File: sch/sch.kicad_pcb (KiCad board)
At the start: 2 copper layers, 98.6 x 49.8 mm, 106 parts, among them P1 SWD, P10 Button_on, P11 LiFePo4, P12 3.3v, P13 SPEAKR, P14 RESET, P15 GPS_UART0, P2 UART, P3 usb, P4 btns1, P5 Leds_gnd, P6 btns2, P7 Leds, P8 3V_bat, P9 LCD, Q1 Q_PMOS_GSD, Q2 Q_PMOS_GSD, Q3 Q_NMOS_DSG, SW1 SW_PUSH, U1 24C512, U10 STMPS2141STR, U11 MCP73123, U12 LT1613, U13 74LVC1G17, U14 74LVC2G74, U15 74LVC1G02, U16 NCP1450, U17 microSD, U2 STM32F401RETx, U3 74HC595, U4 LSM303D, U5 ML8088se, U6 GPS_ANTENNA, U7 INA138, U8 INA138, U9 74LVC1G32, Y1 8MHz, Y2 32768

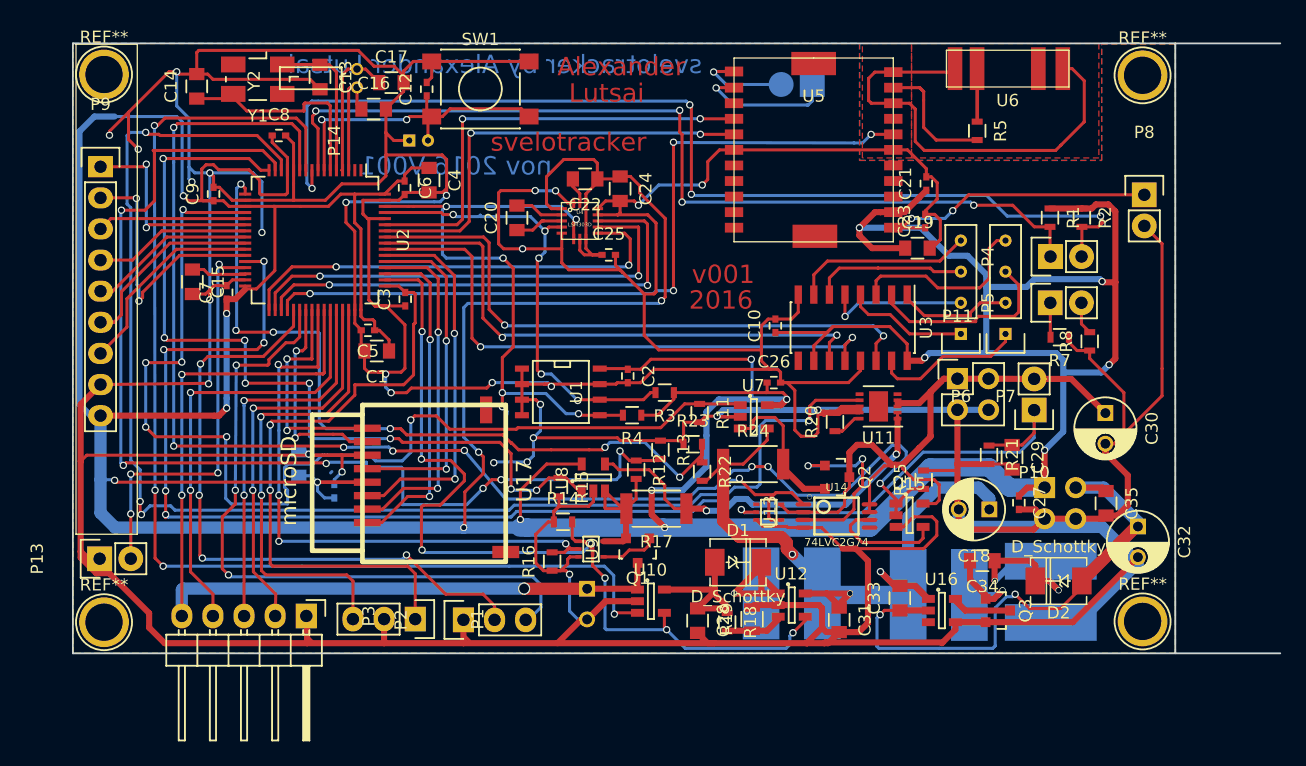
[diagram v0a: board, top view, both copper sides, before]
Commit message: sd card 180 degree rotation
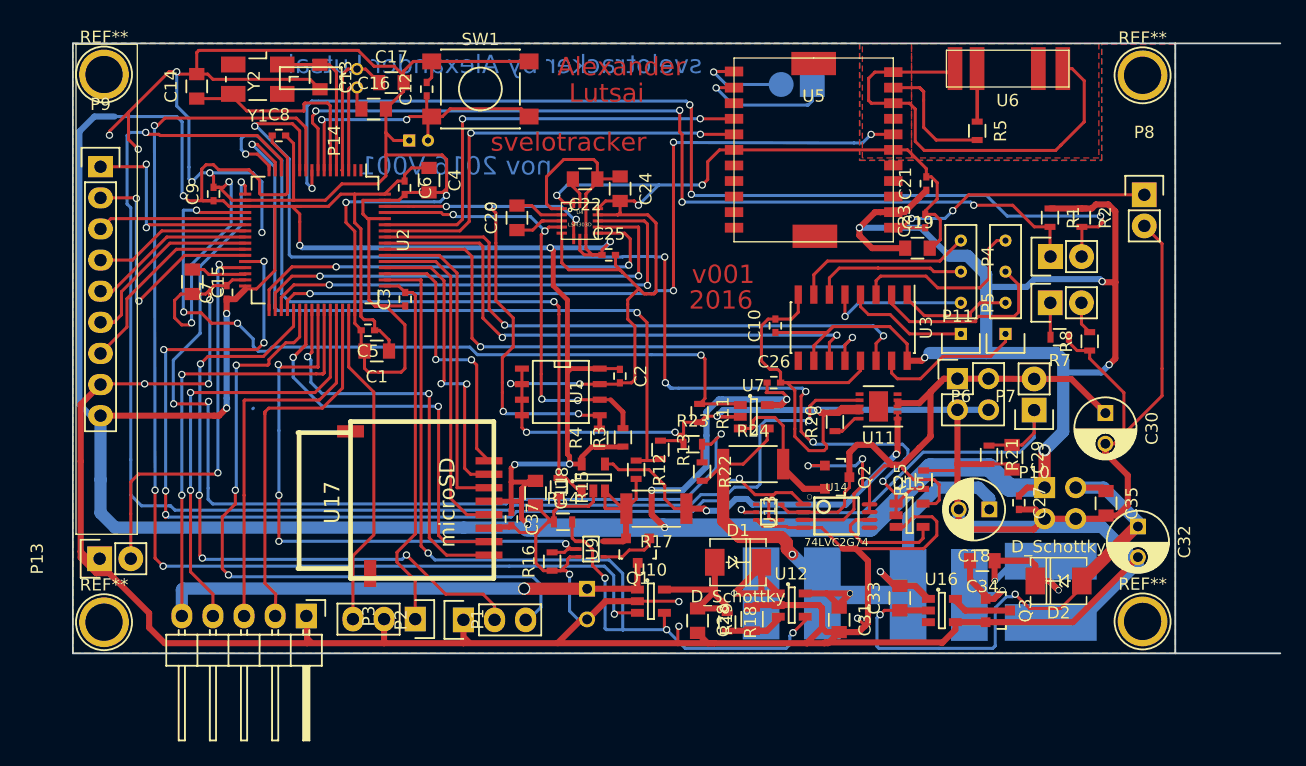
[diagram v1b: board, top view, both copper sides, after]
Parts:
- C11, C37: moved to F.Cu
- moved C11 19.5 mm to (62.7, 130.2), turned to 270 degrees
- moved C37 14.6 mm to (60.7, 132.3), turned to 270 degrees
- moved R3 4.99 mm to (69.8, 125.6), turned to 90 degrees
- moved U17 3.59 mm to (55.5, 130.9), turned to 90 degrees
- moved R4 3.25 mm to (67.9, 125.7), turned to 90 degrees
- moved C2 0.65 mm to (69.5, 120.6)
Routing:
- net GND: track 838.8 -> 788.0 mm, vias 28 -> 26
- net +3V3: track 481.3 -> 447.3 mm, vias 18 -> 17
- net /Sheet5813F141/VUIN: track 89.8 -> 61.4 mm, vias 6 -> 2
- net /Sheet5813F141/ISCH: track 88.4 -> 65.4 mm, vias 6 -> 4
- net /S_D0: track 17.4 -> 37.9 mm
- net /SWCLK: track 50.8 -> 30.5 mm, vias 2 -> 0
- net /Sheet5813F141/SHDN: track 115.0 -> 95.3 mm, vias 8 -> 6
- net /Sheet5813F141/VBAT: track 64.0 -> 81.7 mm, vias 6 -> 4
- net /S_D1: track 18.5 -> 33.4 mm
- net /Sheet5813F141/IUIN: track 70.0 -> 58.6 mm, vias 8 -> 2
- net /SWDIO: track 38.2 -> 26.8 mm, vias 2 -> 0
- net /S_D2: track 27.4 -> 22.5 mm
- net /S_CMD: track 30.7 -> 26.6 mm, vias 2 -> 0
- net /I2C1_SDA: track 52.0 -> 48.3 mm, vias 6 -> 5
- net /S_D3: track 28.3 -> 25.0 mm
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
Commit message: via size for rezonit
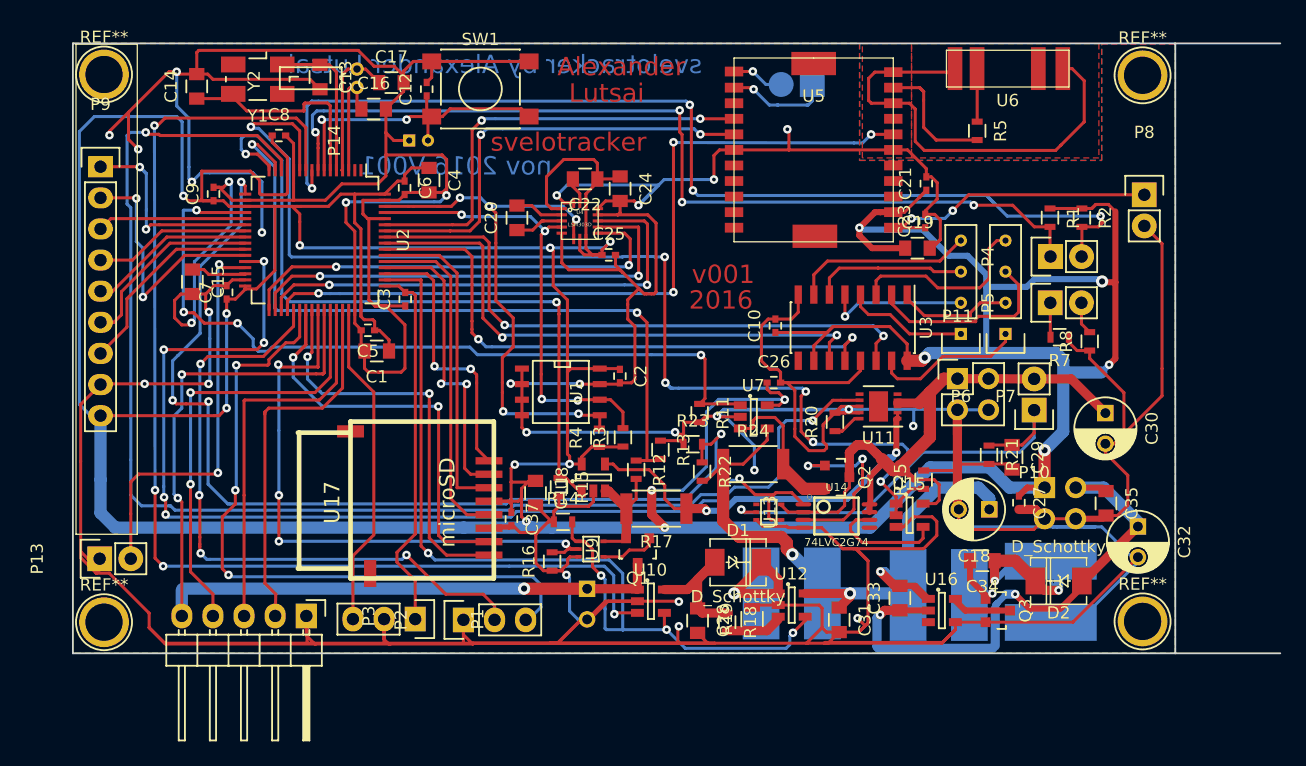
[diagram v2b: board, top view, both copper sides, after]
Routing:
- net GND: track 788.0 -> 816.2 mm, vias 26 -> 28
- net /Sheet5813F141/Isch1: track 66.8 -> 83.5 mm
- net Net-(C32-Pad1): track 44.8 -> 51.6 mm
- net Net-(C30-Pad1): track 56.5 -> 60.9 mm
- net Net-(D1-Pad2): track 15.0 -> 19.1 mm
- net Net-(P15-Pad2): track 7.62 -> 4.29 mm
- net /I2C1_SDA: track 48.3 -> 45.4 mm
- net Net-(P15-Pad1): track 11.4 -> 8.47 mm
- net /Sheet5813F141/Iuin1: track 31.7 -> 34.5 mm
- net /I2C1_SCL: track 37.6 -> 40.2 mm
- net Net-(C34-Pad1): track 16.5 -> 18.4 mm
- net Net-(C28-Pad1): track 13.6 -> 11.9 mm
- net /Sheet5813F141/CH_STAT: track 94.7 -> 93.1 mm
- net /C_INT1: track 40.5 -> 41.8 mm
- net Net-(C34-Pad2): track 8.18 -> 8.99 mm
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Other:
- net class Default: via_dia 0.6 -> 0.7; via_drill 0.4 -> 0.3
- net class vusb added: clearance 0.2, trace_width 0.75, via_dia 1, via_drill 0.5
- rule via_min_size: 0.4 -> 0.7
